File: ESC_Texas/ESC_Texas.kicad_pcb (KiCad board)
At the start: 4 copper layers, 25 parts, among them IC1 UCC21331CQDRQ1, Q1 IPD100N06S4, Q2 IPD100N06S4

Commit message: Initial design
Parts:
- added C1: 12pF, Capacitor_SMD:C_0805_2012Metric, F.Cu at (122.0, 64.1)
- added C10: 100pF, Capacitor_SMD:C_0805_2012Metric, F.Cu at (130.9, 67.1)
- added C11: 100pF, Capacitor_SMD:C_0805_2012Metric, F.Cu at (130.9, 70.2)
- added C12: 100nF, Capacitor_SMD:C_0805_2012Metric, F.Cu at (130.9, 73.2)
- added C13: 4.7uF, Capacitor_SMD:C_0805_2012Metric, F.Cu at (135.4, 64.1)
- added C14: 4.7uF, Capacitor_SMD:C_0805_2012Metric, F.Cu at (135.4, 67.1)
- added C2: 12pF, Capacitor_SMD:C_0805_2012Metric, F.Cu at (122.0, 67.1)
- added C3: 12pF, Capacitor_SMD:C_0805_2012Metric, F.Cu at (122.0, 70.2)
- added C4: 12pF, Capacitor_SMD:C_0805_2012Metric, F.Cu at (122.0, 73.2)
- added C5: 100nF, Capacitor_SMD:C_0805_2012Metric, F.Cu at (126.5, 64.1)
- added C6: 4.7uF, Capacitor_SMD:C_0805_2012Metric, F.Cu at (126.5, 67.1)
- added C7: 820pF, Capacitor_SMD:C_0805_2012Metric, F.Cu at (126.5, 70.2)
- added C8: 0.5pf, Capacitor_SMD:C_0805_2012Metric, F.Cu at (126.5, 73.2)
- added C9: 0.5pF, Capacitor_SMD:C_0805_2012Metric, F.Cu at (130.9, 64.1)
- added C_VCC2: 0.8pF, Capacitor_SMD:C_0805_2012Metric, F.Cu at (135.4, 70.2)
- added C_VCC3: 1uF, Capacitor_SMD:C_0805_2012Metric, F.Cu at (135.4, 73.2)
- added L1: 4.7nH, Inductor_SMD:L_1008_2520Metric_Pad1.43x2.20mm_HandSolder, F.Cu at (132.5, 76.5)
- added U1: nRF52840, Package_DFN_QFN:Nordic_AQFN-73-1EP_7x7mm_P0.5mm, F.Cu at (124.8, 79.7)
- added Y1: 32MHz, Oscillator:Oscillator_SMD_ECS_2520MV-xxx-xx-4Pin_2.5x2.0mm, F.Cu at (131.8, 80.6)
- C_IN1, C_IN2, C_IN3: value C -> 33pF
- C_VDD_B1: value C -> 10uF
- RR_ON_B1, R_ON_A1: value R -> 4.7
- R_BOOT_A1: value R -> 6.8
- R_DT1: value R -> 20k
- R_GS_A1, R_GS_B1: value R -> 10k
- R_INA1, R_INB1: value R -> 47
- R_OFF_A1: value R -> 0
- R_OFF_B1: value R -> R=0
- moved C_VDD_B1 3.00 mm to (149.0, 79.0)
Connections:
- net /Driver_subsheet_1/SW renamed /Driver_subsheet_1/VSSA
- net Net-(D2-K) renamed /Driver_subsheet_1/VDDA
- net Net-(IC1-DT) renamed /Driver_subsheet_1/DT
- net Net-(IC1-INA) renamed /Driver_subsheet_1/INA
- net Net-(IC1-INB) renamed /Driver_subsheet_1/INB
- net Net-(IC1-OUTA) renamed /Driver_subsheet_1/OUTA
- net Net-(IC1-OUTB) renamed /Driver_subsheet_1/OUTB
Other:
- board outline added: 110 x 57 mm

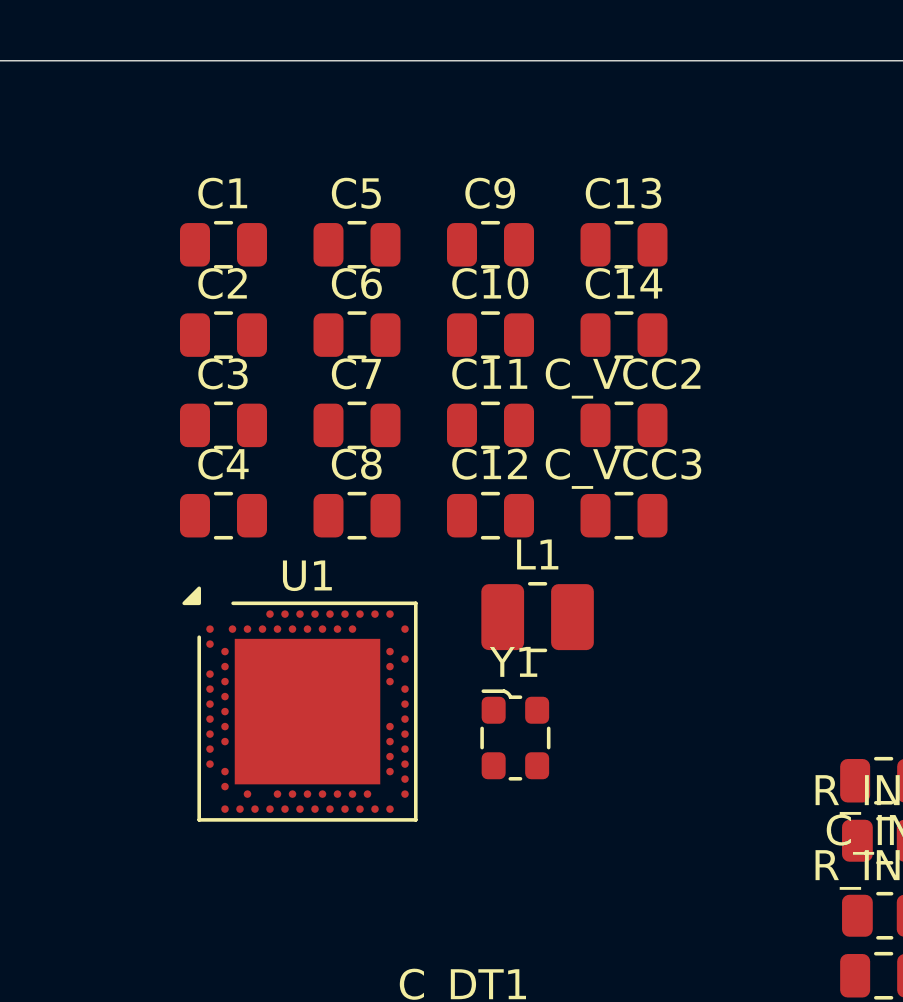
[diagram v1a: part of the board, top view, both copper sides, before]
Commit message: Added text: VDD=15V
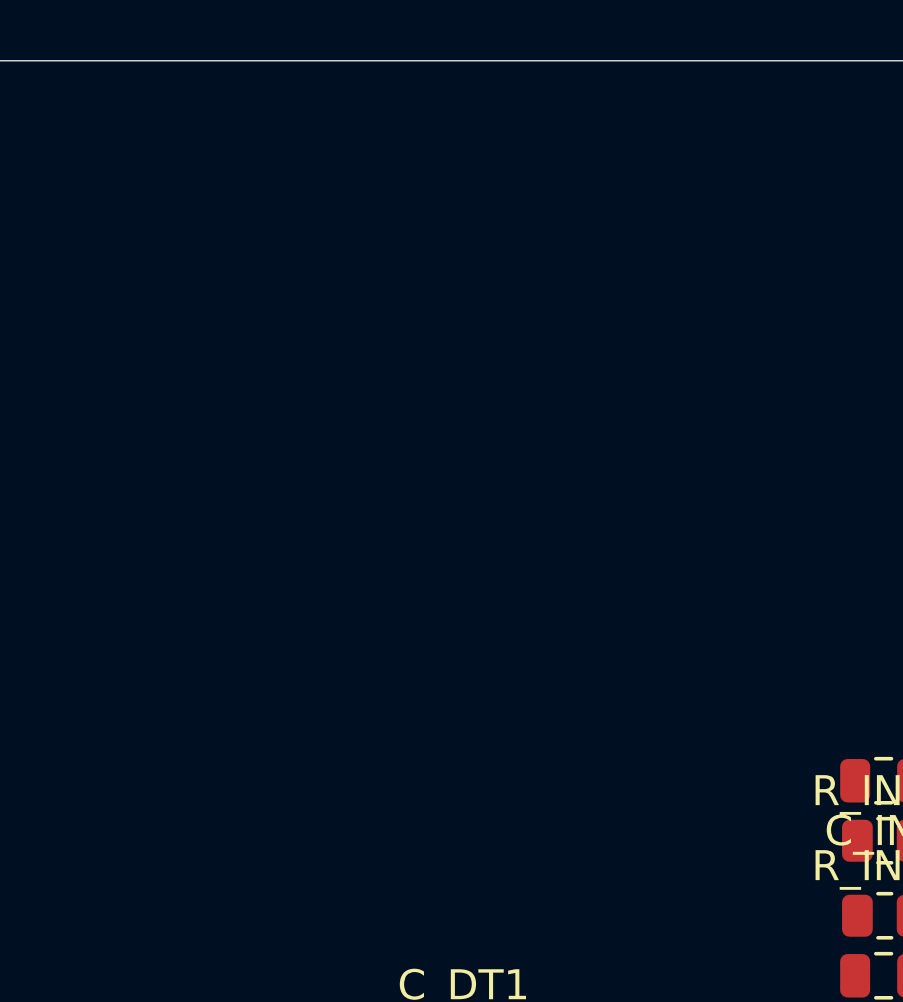
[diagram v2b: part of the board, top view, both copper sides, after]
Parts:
- removed C1, C2, C3, C4: 12pF, Capacitor_SMD:C_0805_2012Metric
- removed C10, C11: 100pF, Capacitor_SMD:C_0805_2012Metric
- removed C12, C5: 100nF, Capacitor_SMD:C_0805_2012Metric
- removed C13, C14, C6: 4.7uF, Capacitor_SMD:C_0805_2012Metric
- removed C7: 820pF, Capacitor_SMD:C_0805_2012Metric
- removed C8: 0.5pf, Capacitor_SMD:C_0805_2012Metric
- removed C9: 0.5pF, Capacitor_SMD:C_0805_2012Metric
- removed C_VCC2: 0.8pF, Capacitor_SMD:C_0805_2012Metric
- removed C_VCC3: 1uF, Capacitor_SMD:C_0805_2012Metric
- removed L1: 4.7nH, Inductor_SMD:L_1008_2520Metric_Pad1.43x2.20mm_HandSolder
- removed U1: nRF52840, Package_DFN_QFN:Nordic_AQFN-73-1EP_7x7mm_P0.5mm
- removed Y1: 32MHz, Oscillator:Oscillator_SMD_ECS_2520MV-xxx-xx-4Pin_2.5x2.0mm
- C_IN1, C_IN2, C_IN3: value 33pF -> C
- C_VDD_B1: value 10uF -> C
- RR_ON_B1, R_ON_A1: value 4.7 -> R
- R_BOOT_A1: value 6.8 -> R
- R_DT1: value 20k -> R
- R_GS_A1, R_GS_B1: value 10k -> R
- R_INA1, R_INB1: value 47 -> R
- R_OFF_A1: value 0 -> R
- R_OFF_B1: value R=0 -> R

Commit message: Saved project after footprints/symbols addition
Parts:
- added C1: 12pF, Capacitor_SMD:C_0805_2012Metric, F.Cu at (111.7, 60.4)
- added C10: 100pF, Capacitor_SMD:C_0805_2012Metric, F.Cu at (120.6, 63.4)
- added C11: 100pF, Capacitor_SMD:C_0805_2012Metric, F.Cu at (120.6, 66.4)
- added C12: 100nF, Capacitor_SMD:C_0805_2012Metric, F.Cu at (120.6, 69.4)
- added C13: 4.7uF, Capacitor_SMD:C_0805_2012Metric, F.Cu at (125.1, 60.4)
- added C14: 4.7uF, Capacitor_SMD:C_0805_2012Metric, F.Cu at (125.1, 63.4)
- added C2: 12pF, Capacitor_SMD:C_0805_2012Metric, F.Cu at (111.7, 63.4)
- added C3: 12pF, Capacitor_SMD:C_0805_2012Metric, F.Cu at (111.7, 66.4)
- added C4: 12pF, Capacitor_SMD:C_0805_2012Metric, F.Cu at (111.7, 69.4)
- added C5: 100nF, Capacitor_SMD:C_0805_2012Metric, F.Cu at (116.2, 60.4)
- added C6: 4.7uF, Capacitor_SMD:C_0805_2012Metric, F.Cu at (116.2, 63.4)
- added C7: 820pF, Capacitor_SMD:C_0805_2012Metric, F.Cu at (116.2, 66.4)
- added C8: 0.5pf, Capacitor_SMD:C_0805_2012Metric, F.Cu at (116.2, 69.4)
- added C9: 0.5pF, Capacitor_SMD:C_0805_2012Metric, F.Cu at (120.6, 60.4)
- added C_VCC2: 0.8pF, Capacitor_SMD:C_0805_2012Metric, F.Cu at (125.1, 66.4)
- added C_VCC3: 1uF, Capacitor_SMD:C_0805_2012Metric, F.Cu at (125.1, 69.4)
- added L1: 4.7nH, Inductor_SMD:L_1008_2520Metric_Pad1.43x2.20mm_HandSolder, F.Cu at (122.2, 77.1)
- added U1: nRF52840, Package_DFN_QFN:Nordic_AQFN-73-1EP_7x7mm_P0.5mm, F.Cu at (114.5, 75.9)
- added Y1: 32MHz, Oscillator:Oscillator_SMD_ECS_2520MV-xxx-xx-4Pin_2.5x2.0mm, F.Cu at (121.5, 73.1)
- added Y2: 32MHz, Oscillator:Oscillator_SMD_ECS_2520MV-xxx-xx-4Pin_2.5x2.0mm, F.Cu at (125.3, 73.1)
- C_IN1, C_IN2, C_IN3: value C -> 33pF
- C_VDD_B1: value C -> 10uF
- IC1: footprint UCC21331CDR:SOIC127P600X175-16N -> LIB_UCC21331CQDRQ1:SOIC127P600X175-16N
- PS1: footprint MP-k78U15:MPK78U15500R3L -> MP-K78U15-500R3L:MPK78U15500R3L
- RR_ON_B1, R_ON_A1: value R -> 4.7
- R_BOOT_A1: value R -> 6.8
- R_DT1: value R -> 20k
- R_GS_A1, R_GS_B1: value R -> 10k
- R_INA1, R_INB1: value R -> 47
- R_OFF_A1: value R -> 0
- R_OFF_B1: value R -> R=0

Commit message: Save
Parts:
- added L1: 4.7nH, Inductor_SMD:L_1008_2520Metric_Pad1.43x2.20mm_HandSolder, F.Cu at (132.8, 77.0)
- Y2: value 32MHz -> 32.768kHz
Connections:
- U1 pad AC5: Net-(U1-DECUSB) -> unconnected-(U1-DECUSB-PadAC5)
- U1 pad AD2: VBUS -> GND
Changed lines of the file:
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@@
 	(net 87 "unconnected-(U1-D+-PadAD6)")
 	(net 88 "unconnected-(U1-P0.16-PadAC11)")
+	(net 89 "unconnected-(U1-DECUSB-PadAC5)")
 	(footprint "Capacitor_SMD:C_0805_2012Metric"
 		(layer "F.Cu")
@@
 		)
 	)
+	(footprint "Inductor_SMD:L_1008_2520Metric_Pad1.43x2.20mm_HandSolder"
+		(layer "F.Cu")
+		(at 132.8375 77)
+		(descr "Inductor SMD 1008 (2520 Metric), square (rectangular) end terminal, IPC_7351 nominal with elongated pad for handsoldering. (Body size source: https://ecsxtal.com/store/pdf/ECS-MPI2520-SMD-POWER-INDUCTOR.pdf), generated with kicad-footprint-generator")
+		(tags "inductor handsolder")
+		(property "Reference" "L1"
+			(at 0 -2.05 0)
+			(layer "F.SilkS")
+			(effects
+				(font
+					(size 1 1)
+					(thickness 0.15)
+				)
+			)
+		)
+		(property "Value" "4.7nH"
+			(at 0 2.05 0)
+			(layer "F.Fab")
+			(effects
+				(font
+					(size 1 1)
+					(thickness 0.15)
+				)
+			)
+		)
+		(property "Footprint" "Inductor_SMD:L_1008_2520Metric_Pad1.43x2.20mm_HandSolder"
+			(at 0 0 0)
+			(unlocked yes)
+			(layer "F.Fab")
+			(hide yes)
+			(effects
+				(font
+					(size 1.27 1.27)
+					(thickness 0.15)
+				)
+			)
+		)
+		(property "Datasheet" ""
+			(at 0 0 0)
+			(unlocked yes)
+			(layer "F.Fab")
+			(hide yes)
+			(effects
+				(font
+					(size 1.27 1.27)
+					(thickness 0.15)
+				)
+			)
+		)
+		(property "Description" "Inductor"
+			(at 0 0 0)
+			(unlocked yes)
+			(layer "F.Fab")
+			(hide yes)
+			(effects
+				(font
+					(size 1.27 1.27)
+					(thickness 0.15)
+				)
+			)
+		)
+		(property ki_fp_filters "Choke_* *Coil* Inductor_* L_*")
+		(sheetname "Root")
+		(sheetfile "ESC_Texas.kicad_sch")
+		(attr smd)
+		(fp_line
+			(start -0.261252 -1.11)
+			(end 0.261252 -1.11)
+			(stroke
+				(width 0.12)
+				(type solid)
+			)
+			(layer "F.SilkS")
+		)
+		(fp_line
+			(start -0.261252 1.11)
+			(end 0.261252 1.11)
+			(stroke
+				(width 0.12)
+				(type solid)
+			)
+			(layer "F.SilkS")
+		)
+		(fp_line
+			(start -2.12 -1.35)
+			(end 2.12 -1.35)
+			(stroke
+				(width 0.05)
+				(type solid)
+			)
+			(layer "F.CrtYd")
+		)
+		(fp_line
+			(start -2.12 1.35)
+			(end -2.12 -1.35)
+			(stroke
+				(width 0.05)
+				(type solid)
+			)
+			(layer "F.CrtYd")
+		)
+		(fp_line
+			(start 2.12 -1.35)
+			(end 2.12 1.35)
+			(stroke
+				(width 0.05)
+				(type solid)
+			)
+			(layer "F.CrtYd")
+		)
+		(fp_line
+			(start 2.12 1.35)
+			(end -2.12 1.35)
+			(stroke
+				(width 0.05)
+				(type solid)
+			)
+			(layer "F.CrtYd")
+		)
+		(fp_line
+			(start -1.25 -1)
+			(end 1.25 -1)
+			(stroke
+				(width 0.1)
+				(type solid)
+			)
+			(layer "F.Fab")
+		)
+		(fp_line
+			(start -1.25 1)
+			(end -1.25 -1)
+			(stroke
+				(width 0.1)
+				(type solid)
+			)
+			(layer "F.Fab")
+		)
+		(fp_line
+			(start 1.25 -1)
+			(end 1.25 1)
+			(stroke
+				(width 0.1)
+				(type solid)
+			)
+			(layer "F.Fab")
+		)
+		(fp_line
+			(start 1.25 1)
+			(end -1.25 1)
+			(stroke
+				(width 0.1)
+				(type solid)
+			)
+			(layer "F.Fab")
+		)
+		(fp_text user "${REFERENCE}"
+			(at 0 0 0)
+			(layer "F.Fab")
+			(effects
+				(font
+					(size 0.62 0.62)
+					(thickness 0.09)
+				)
+			)
+		)
+		(pad "1" smd roundrect
+			(at -1.1625 0)
+			(size 1.425 2.2)
+			(layers "F.Cu" "F.Paste" "F.Mask")
+			(roundrect_rratio 0.175439)
+			(net 29 "Net-(C8-Pad2)")
+			(pinfunction "1")
+			(pintype "passive")
+		)
+		(pad "2" smd roundrect
+			(at 1.1625 0)
+			(size 1.425 2.2)
+			(layers "F.Cu" "F.Paste" "F.Mask")
+			(roundrect_rratio 0.175439)
+			(net 36 "Net-(U1-ANT)")
+			(pinfunction "2")
+			(pintype "passive")
+		)
+		(model "${KICAD8_3DMODEL_DIR}/Inductor_SMD.3dshapes/L_1008_2520Metric.wrl"
+			(offset
+				(xyz 0 0 0)
+			)
+			(scale
+				(xyz 1 1 1)
+			)
+			(rotate
+				(xyz 0 0 0)
+			)
+		)
+	)
 	(footprint "Capacitor_SMD:C_0805_2012Metric"
 		(layer "F.Cu")
@@
 			(property pad_prop_bga)
 			(layers "F.Cu" "F.Paste" "F.Mask")
-			(net 34 "Net-(U1-DECUSB)")
+			(net 89 "unconnected-(U1-DECUSB-PadAC5)")
 			(pinfunction "DECUSB")
-			(pintype "passive")
+			(pintype "passive+no_connect")
 		)
 		(pad "AC9" smd circle
@@
 			(property pad_prop_bga)
 			(layers "F.Cu" "F.Paste" "F.Mask")
-			(net 35 "VBUS")
+			(net 14 "GND")
 			(pinfunction "VBUS")
 			(pintype "power_in")
@@
 			)
 		)
-		(property "Value" "32MHz"
+		(property "Value" "32.768kHz"
 			(at 0 2.5 0)
 			(layer "F.Fab")

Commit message: Before adding footprint
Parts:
- moved C6 19.7 mm to (111.5, 82.5), turned to 180 degrees
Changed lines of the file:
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@@
 	(footprint "Capacitor_SMD:C_0805_2012Metric"
 		(layer "F.Cu")
-		(at 116.185 63.395)
+		(at 111.5 82.5 180)
 		(descr "Capacitor SMD 0805 (2012 Metric), square (rectangular) end terminal, IPC_7351 nominal, (Body size source: IPC-SM-782 page 76, https://www.pcb-3d.com/wordpress/wp-content/uploads/ipc-sm-782a_amendment_1_and_2.pdf, https://docs.google.com/spreadsheets/d/1BsfQQcO9C6DZCsRaXUlFlo91Tg2WpOkGARC1WS5S8t0/edit?usp=sharing), generated with kicad-footprint-generator")
 		(tags "capacitor")
 		(property "Reference" "C6"
-			(at 0 -1.68 0)
+			(at 0 -1.68 360)
 			(layer "F.SilkS")
 			(effects
@@
 		)
 		(property "Value" "4.7uF"
-			(at 0 1.68 0)
+			(at 0 1.68 360)
 			(layer "F.Fab")
 			(effects
@@
 		)
 		(property "Footprint" "Capacitor_SMD:C_0805_2012Metric"
-			(at 0 0 0)
+			(at 0 0 180)
 			(unlocked yes)
 			(layer "F.Fab")
@@
 		)
 		(property "Datasheet" ""
-			(at 0 0 0)
+			(at 0 0 180)
 			(unlocked yes)
 			(layer "F.Fab")
@@
 		)
 		(property "Description" "Unpolarized capacitor"
-			(at 0 0 0)
+			(at 0 0 180)
 			(unlocked yes)
 			(layer "F.Fab")
@@
 		(attr smd)
 		(fp_line
+			(start -0.261252 0.735)
+			(end 0.261252 0.735)
+			(stroke
+				(width 0.12)
+				(type solid)
+			)
+			(layer "F.SilkS")
+		)
+		(fp_line
 			(start -0.261252 -0.735)
 			(end 0.261252 -0.735)
@@
 		)
 		(fp_line
-			(start -0.261252 0.735)
-			(end 0.261252 0.735)
+			(start 1.7 0.98)
+			(end -1.7 0.98)
 			(stroke
-				(width 0.12)
+				(width 0.05)
 				(type solid)
 			)
-			(layer "F.SilkS")
+			(layer "F.CrtYd")
 		)
 		(fp_line
-			(start -1.7 -0.98)
-			(end 1.7 -0.98)
+			(start 1.7 -0.98)
+			(end 1.7 0.98)
 			(stroke
 				(width 0.05)
@@
 		)
 		(fp_line
-			(start 1.7 -0.98)
-			(end 1.7 0.98)
+			(start -1.7 -0.98)
+			(end 1.7 -0.98)
 			(stroke
 				(width 0.05)
@@
 		)
 		(fp_line
-			(start 1.7 0.98)
-			(end -1.7 0.98)
+			(start 1 0.625)
+			(end -1 0.625)
 			(stroke
-				(width 0.05)
+				(width 0.1)
 				(type solid)
 			)
-			(layer "F.CrtYd")
+			(layer "F.Fab")
 		)
 		(fp_line
-			(start -1 -0.625)
-			(end 1 -0.625)
+			(start 1 -0.625)
+			(end 1 0.625)
 			(stroke
 				(width 0.1)
@@
 		)
 		(fp_line
-			(start 1 -0.625)
-			(end 1 0.625)
-			(stroke
-				(width 0.1)
-				(type solid)
-			)
-			(layer "F.Fab")
-		)
-		(fp_line
-			(start 1 0.625)
-			(end -1 0.625)
+			(start -1 -0.625)
+			(end 1 -0.625)
 			(stroke
 				(width 0.1)
@@
 		)
 		(fp_text user "${REFERENCE}"
-			(at 0 0 0)
+			(at 0 0 360)
 			(layer "F.Fab")
 			(effects
@@
 		)
 		(pad "1" smd roundrect
-			(at -0.95 0)
+			(at -0.95 0 180)
 			(size 1 1.45)
 			(layers "F.Cu" "F.Paste" "F.Mask")
@@
 		)
 		(pad "2" smd roundrect
-			(at 0.95 0)
+			(at 0.95 0 180)
 			(size 1 1.45)
 			(layers "F.Cu" "F.Paste" "F.Mask")

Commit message: Cleaned schamatic again
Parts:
- added C13: 12pF, Capacitor_SMD:C_0805_2012Metric, F.Cu at (1.73, 1.00)
- added C20: 12pF, Capacitor_SMD:C_0805_2012Metric, F.Cu at (1.73, 4.01)
- added C21: 100nF, Capacitor_SMD:C_0805_2012Metric, F.Cu at (1.73, 7.03)
- added C25: 100nF, Capacitor_SMD:C_0805_2012Metric, F.Cu at (1.73, 10.0)
- added C26: 100nF, Capacitor_SMD:C_0805_2012Metric, F.Cu at (1.73, 13.0)
- added C27: 100nF, Capacitor_SMD:C_0805_2012Metric, F.Cu at (1.73, 16.1)
- added C28: 100nF, Capacitor_SMD:C_0805_2012Metric, F.Cu at (6.17, 1.00)
- added C29: 100nF, Capacitor_SMD:C_0805_2012Metric, F.Cu at (6.17, 4.01)
- added C30: 12pF, Capacitor_SMD:C_0805_2012Metric, F.Cu at (6.17, 7.03)
- added C31: 12pF, Capacitor_SMD:C_0805_2012Metric, F.Cu at (6.17, 10.0)
- added C32: 1uF, Capacitor_SMD:C_0805_2012Metric, F.Cu at (6.17, 13.0)
- added C33: 47nF, Capacitor_SMD:C_0805_2012Metric, F.Cu at (6.17, 16.1)
- added C34: 1.2pF, Capacitor_SMD:C_0805_2012Metric, F.Cu at (10.6, 1.00)
- added C35: 100pF, Capacitor_SMD:C_0805_2012Metric, F.Cu at (10.6, 4.01)
- added C36: 1pF, Capacitor_SMD:C_0805_2012Metric, F.Cu at (10.6, 7.03)
- added IC5: nRF52840-QFAA-F-R7, nRF52840-QFAA-F-R7:QFN40P600X600X95-49N-D, F.Cu at (17.0, 18.6)
- added L4: 15nH, Inductor_SMD:L_1008_2520Metric_Pad1.43x2.20mm_HandSolder, F.Cu at (15.5, 1.38)
- added L5: 10uH, Inductor_SMD:L_1008_2520Metric_Pad1.43x2.20mm_HandSolder, F.Cu at (15.5, 5.12)
- added L6: 4.7nH, Inductor_SMD:L_1008_2520Metric_Pad1.43x2.20mm_HandSolder, F.Cu at (15.5, 8.88)
- added L7: 2.2nH, Inductor_SMD:L_1008_2520Metric_Pad1.43x2.20mm_HandSolder, F.Cu at (15.5, 12.6)
- added Y5: LFSPXO009686, LFSPXO009686:LFSPXO009686, F.Cu at (2.36, 20.2)
- added Y6: 32MHz, Oscillator:Oscillator_SMD_ECS_2520MV-xxx-xx-4Pin_2.5x2.0mm, F.Cu at (7.12, 19.7)
- renumbered D4 to D8, PS1 to PS3, Q1 to Q5
